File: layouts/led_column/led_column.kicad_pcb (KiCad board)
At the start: 2 copper layers, 10 parts

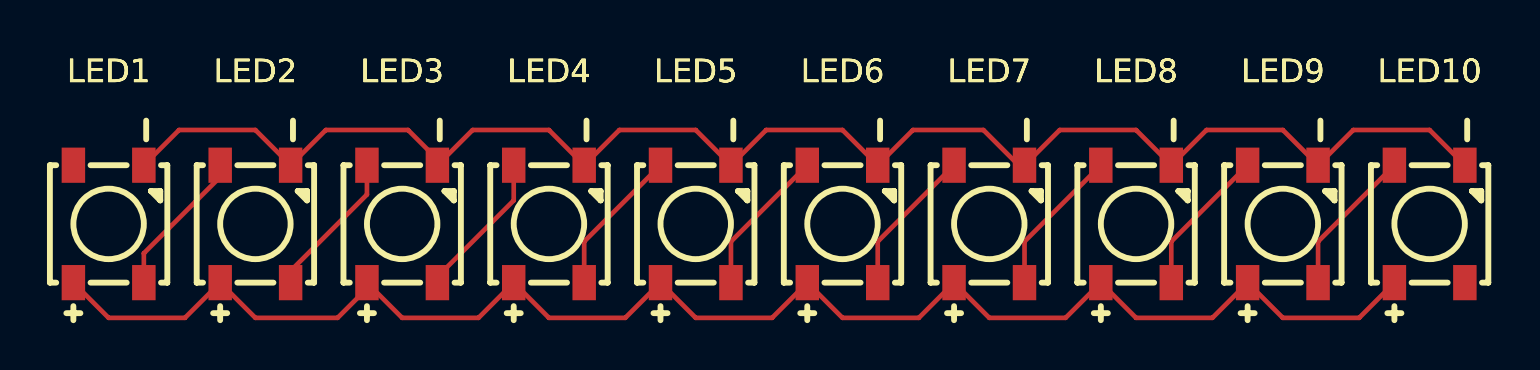
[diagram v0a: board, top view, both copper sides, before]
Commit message: Remove the 5A fuse
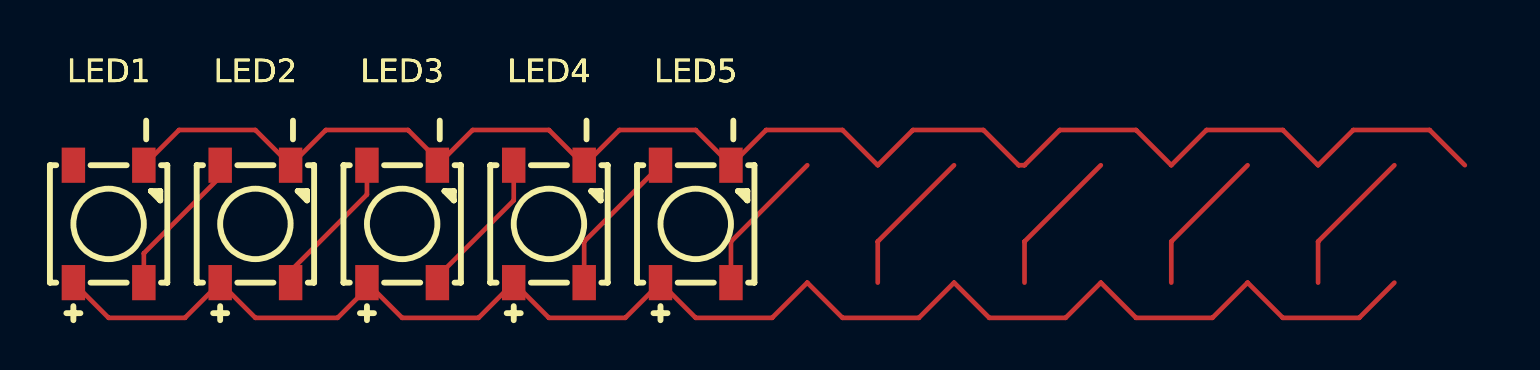
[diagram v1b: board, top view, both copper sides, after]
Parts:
- removed LED10, LED6, LED7, LED8, LED9: , XINGLIGHT_XL_5050RGBC_WS2812B:LED-SMD_4P-L5.0-W5.0-BL_XL-5050RGBC
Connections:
- LED1 pad 2: DIN-2 -> DIN-1
- LED2 pad 2: DOU-4 -> DOU-1
- LED2 pad 4: DIN-2 -> DIN-1
- LED3 pad 2: DOU-3 -> DIN
- LED3 pad 4: DOU-4 -> DOU-1
- LED4 pad 2: DIN-1 -> DOU
- LED4 pad 4: DOU-3 -> DIN
- LED5 pad 2: DOU -> data_out
- LED5 pad 4: DIN-1 -> DOU
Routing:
- net (no net): track 0.00 -> 25.4 mm
- net data_out: track 0.00 -> 6.35 mm
- net DOU-4: track 6.35 -> 0.00 mm
- net DOU-3: track 6.35 -> 0.00 mm
- net DOU-2: track 6.35 -> 0.00 mm
- net DIN-3: track 6.35 -> 0.00 mm
- net DIN-2: track 6.35 -> 0.00 mm

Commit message: remove autogenerated trait, fix fp-lib-table, update gitignore
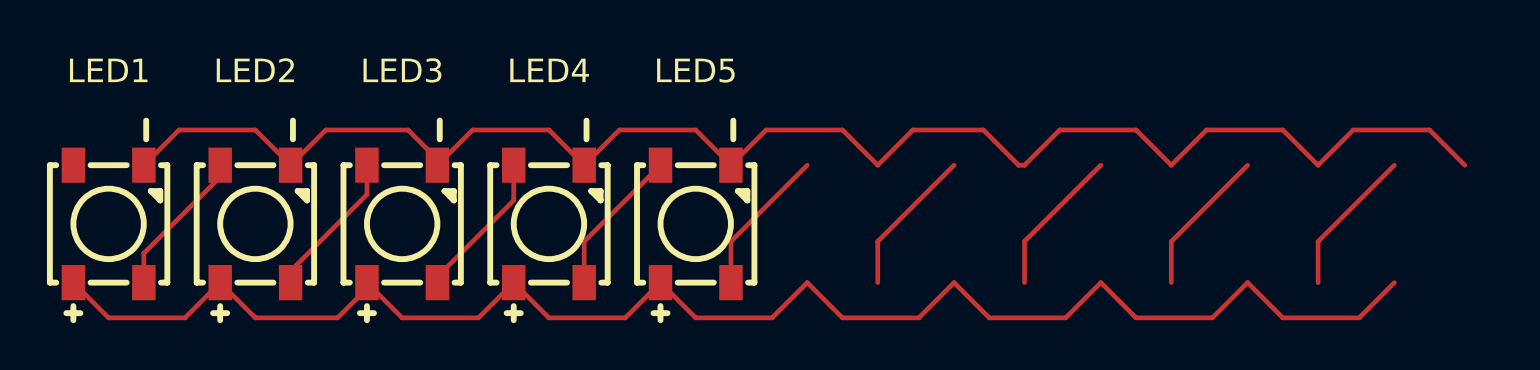
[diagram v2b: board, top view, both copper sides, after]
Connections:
- LED2 pad 2: DOU-1 -> DIN
- LED3 pad 2: DIN -> DOU-1
- LED3 pad 4: DOU-1 -> DIN
- LED4 pad 4: DIN -> DOU-1
